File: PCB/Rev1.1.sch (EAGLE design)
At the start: 2 parts

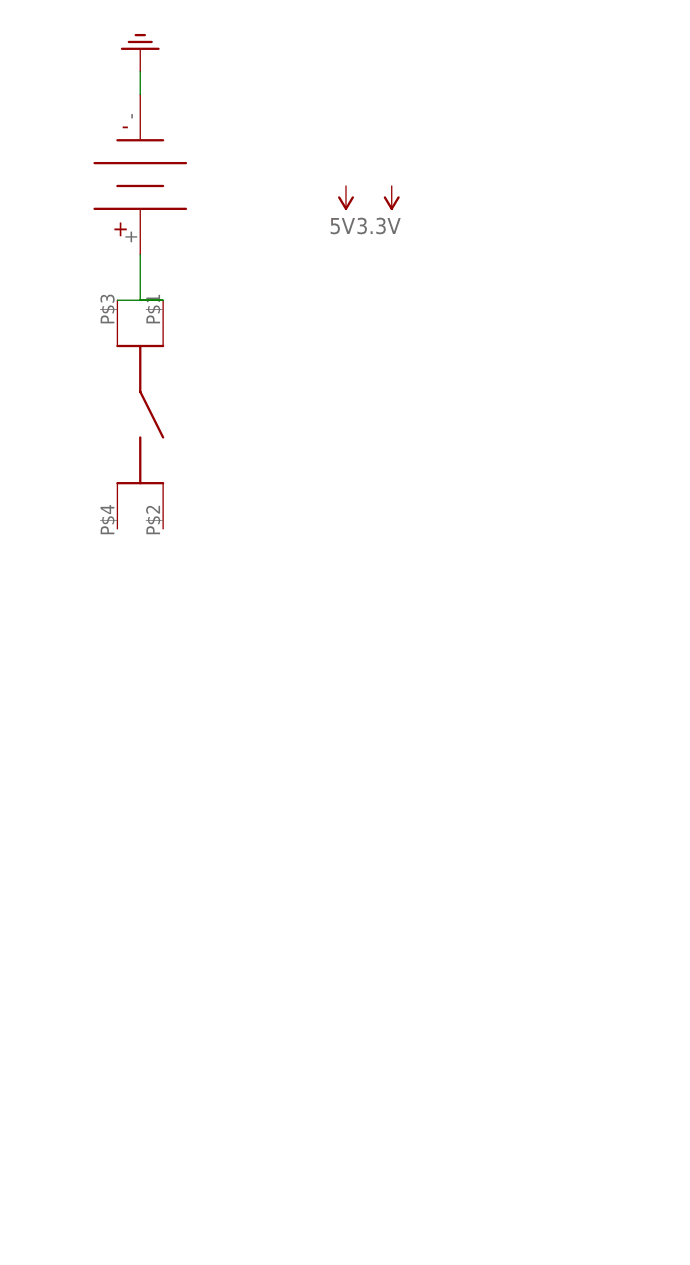
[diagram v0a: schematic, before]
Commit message: Finished power supply schematic.
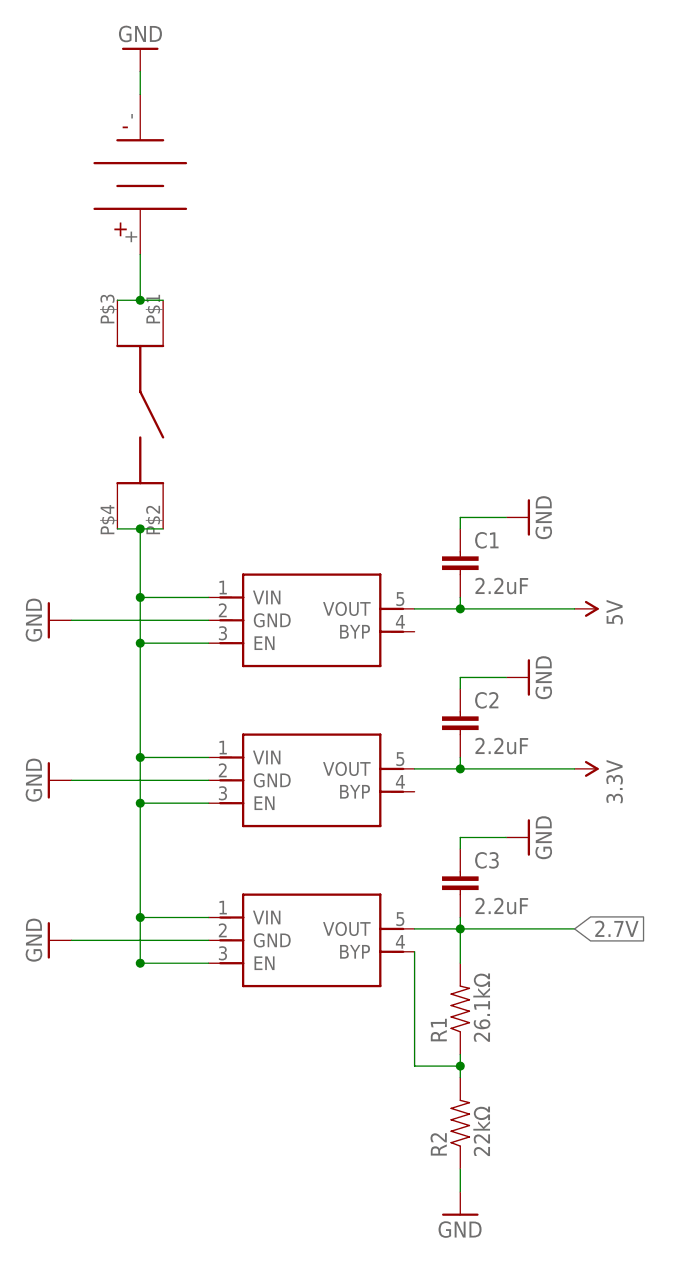
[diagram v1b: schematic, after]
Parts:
- added C1, C2, C3: 2.2uF, SparkFun-Capacitors:CAP0805
- added R1: 26.1kΩ, SparkFun-Resistors:RESISTOR0805-RES
- added R2: 22kΩ, SparkFun-Resistors:RESISTOR0805-RES
- added U$3: 5V Reg, BayouBot:SPX3819
- added U$4: 3.3V Reg, BayouBot:SPX3819
- added U$5: 2.7V Reg, BayouBot:SPX3819
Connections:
- new net 2.7V: C3.2, R1.2, U$5.VOUT
- new net 3.3V: C2.2, U$4.VOUT
- new net 5V: C1.2, U$3.VOUT
- new net N$2: U$2.P$2, U$2.P$4, U$3.EN, U$3.VIN, U$4.EN, U$4.VIN, U$5.EN, U$5.VIN
- new net N$3: R1.1, R2.2, U$5.BYP
- net GND: now also C1.1, C2.1, C3.1, R2.1, U$3.GND, U$4.GND, U$5.GND

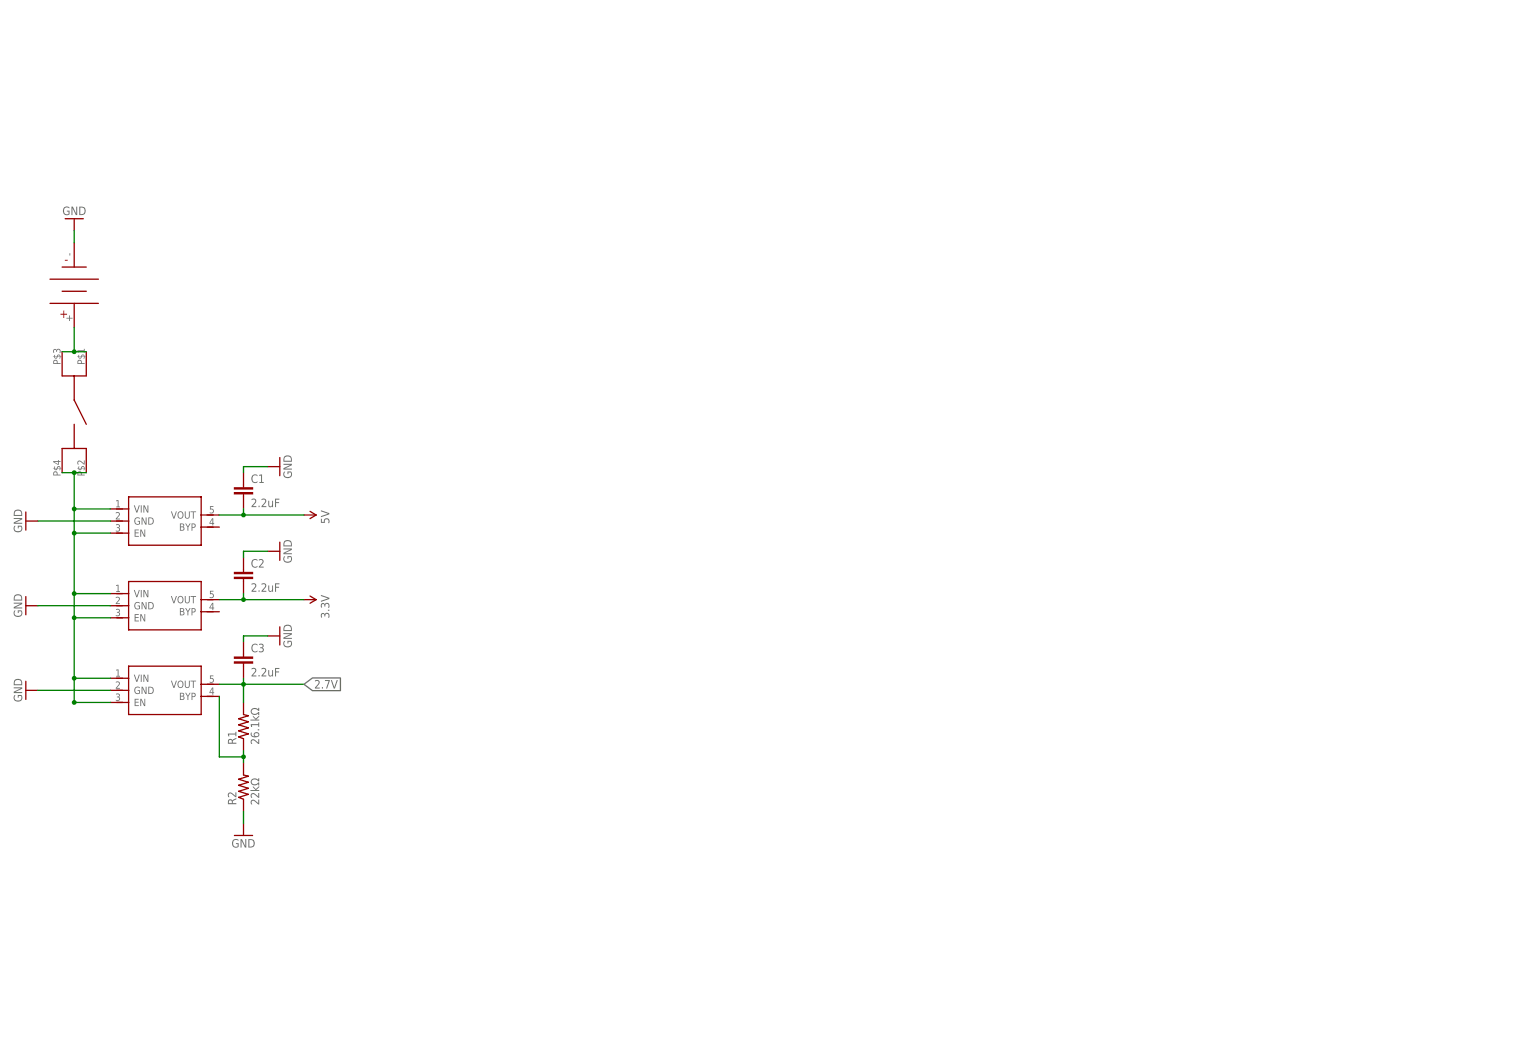
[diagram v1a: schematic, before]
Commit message: Finished schematic for next board revision.
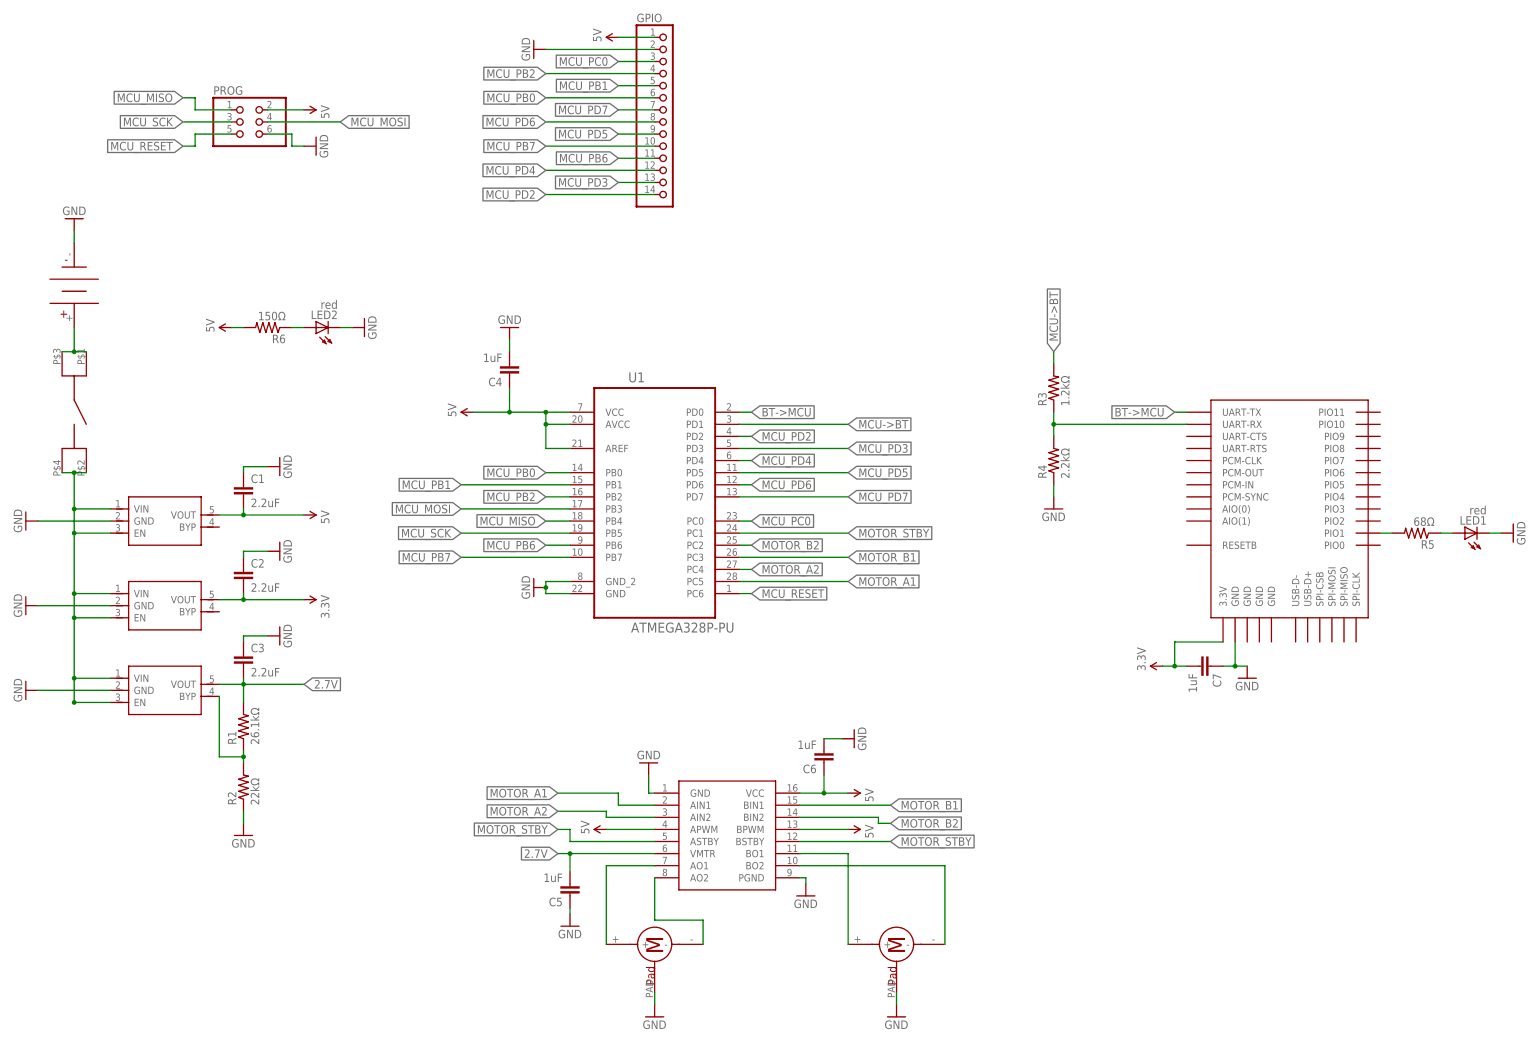
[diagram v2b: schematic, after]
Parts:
- added C4, C5, C6, C7: 1uF, SparkFun-Capacitors:CAP0805
- added GPIO: (no value), pinhead:PINHD-1X14
- added LED1, LED2: red, adafruit:LEDCHIP-LED0805
- added PROG: (no value), pinhead:PINHD-2X3
- added R3: 1.2kΩ, SparkFun-Resistors:RESISTOR0805-RES
- added R4: 2.2kΩ, SparkFun-Resistors:RESISTOR0805-RES
- added R5: 68Ω, SparkFun-Resistors:RESISTOR0805-RES
- added R6: 150Ω, SparkFun-Resistors:RESISTOR0805-RES
- added U$7, U$8: PICO_VIBE_MTR, BayouBot:PICO_VIBE_MTR
- added U1: ATMEGA328P-PU, Atmel_By_element14_Batch_1-00:ATMEGA328P-PU
- added U2: BT, BayouBot:BTM400_6B
- added U3: SMD_H-BRIDGE, BayouBot:SMD_H-BRIDGE
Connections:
- new net BT->MCU: U1.PD0, U2.UART-TX
- new net MCU->BT: R3.2, U1.PD1
- new net MCU_MISO: PROG.1, U1.PB4
- new net MCU_MOSI: PROG.4, U1.PB3
- new net MCU_PB0: GPIO.6, U1.PB0
- new net MCU_PB1: GPIO.5, U1.PB1
- new net MCU_PB2: GPIO.4, U1.PB2
- new net MCU_PB6: GPIO.11, U1.PB6
- new net MCU_PB7: GPIO.10, U1.PB7
- new net MCU_PC0: GPIO.3, U1.PC0
- new net MCU_PD2: GPIO.14, U1.PD2
- new net MCU_PD3: GPIO.13, U1.PD3
- new net MCU_PD4: GPIO.12, U1.PD4
- new net MCU_PD5: GPIO.9, U1.PD5
- new net MCU_PD6: GPIO.8, U1.PD6
- new net MCU_PD7: GPIO.7, U1.PD7
- new net MCU_RESET: PROG.5, U1.PC6
- new net MCU_SCK: PROG.3, U1.PB5
- new net MOTOR_A1: U1.PC5, U3.AIN1
- new net MOTOR_A2: U1.PC4, U3.AIN2
- new net MOTOR_B1: U1.PC3, U3.BIN1
- new net MOTOR_B2: U1.PC2, U3.BIN2
- new net MOTOR_STBY: U1.PC1, U3.ASTBY, U3.BSTBY
- new net N$10: R5.2, U2.PIO1
- new net N$11: LED1.A, R5.1
- new net N$12: LED2.A, R6.1
- new net N$4: U$7.+, U3.AO1
- new net N$5: U$7.-, U3.AO2
- new net N$6: U$8.+, U3.BO1
- new net N$7: U$8.-, U3.BO2
- new net N$8: C5.2, U3.VMTR
- new net N$9: R3.1, R4.2, U2.UART-RX
- net 3.3V: now also C7.2, U2.3.3V
- net 5V: now also C4.1, C6.1, GPIO.1, PROG.2, R6.2, U1.AREF, U1.AVCC, U1.VCC, U3.APWM, U3.BPWM, U3.VCC
- net GND: now also C4.2, C5.1, C6.2, C7.1, GPIO.2, LED1.C, LED2.C, PROG.6, R4.1, U$7.PAD, U$8.PAD, U1.GND, U1.GND_2, U2.GND@1, U3.GND, U3.PGND

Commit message: Routed new PCB version.
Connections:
- removed net N$8: C5.2, U3.VMTR
- net 2.7V: now also C5.2, U3.VMTR
- net MCU_PB0: now also GPIO.14; no longer GPIO.6
- net MCU_PB6: now also GPIO.9; no longer GPIO.11
- net MCU_PD2: now also GPIO.6; no longer GPIO.14
- net MCU_PD3: now also GPIO.7; no longer GPIO.13
- net MCU_PD4: now also GPIO.8; no longer GPIO.12
- net MCU_PD5: now also GPIO.11; no longer GPIO.9
- net MCU_PD6: now also GPIO.12; no longer GPIO.8
- net MCU_PD7: now also GPIO.13; no longer GPIO.7
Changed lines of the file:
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@@
 <setting verticaltext="up"/>
 </settings>
-<grid distance="0.1" unitdist="inch" unit="inch" style="lines" multiple="1" display="no" altdistance="0.05" altunitdist="inch" altunit="inch"/>
+<grid distance="0.1" unitdist="inch" unit="inch" style="lines" multiple="1" display="no" altdistance="0.01" altunitdist="inch" altunit="inch"/>
 <layers>
 <layer number="1" name="Top" color="4" fill="1" visible="no" active="no"/>
@@
 <parts>
 <part name="U$1" library="BayouBot" deviceset="20MM_COIN" device=""/>
-<part name="U$2" library="BayouBot" deviceset="POWER_BTN" device=""/>
 <part name="SUPPLY1" library="SparkFun-Aesthetics" deviceset="5V" device=""/>
 <part name="SUPPLY2" library="SparkFun-Aesthetics" deviceset="3.3V" device=""/>
@@
 <part name="LED2" library="adafruit" deviceset="LED" device="CHIP-LED0805" value="red"/>
 <part name="R6" library="SparkFun-Resistors" deviceset="RESISTOR" device="0805-RES" value="150Ω"/>
+<part name="U$2" library="BayouBot" deviceset="POWER_BTN" device=""/>
 </parts>
 <sheets>
@@
 <instances>
 <instance part="U$1" gate="G$1" x="22.86" y="55.88" rot="R180"/>
-<instance part="U$2" gate="G$1" x="22.86" y="30.48" rot="R270"/>
 <instance part="SUPPLY1" gate="G$1" x="71.12" y="8.89" rot="R270"/>
 <instance part="SUPPLY2" gate="G$1" x="71.12" y="-8.89" rot="R270"/>
@@
 <instance part="LED2" gate="G$1" x="73.66" y="48.26" rot="R90"/>
 <instance part="R6" gate="G$1" x="63.5" y="48.26" rot="R180"/>
+<instance part="U$2" gate="G$1" x="22.86" y="30.48" rot="R270"/>
 </instances>
 <busses>
@@
 <pinref part="U$1" gate="G$1" pin="+"/>
 <wire x1="22.86" y1="48.26" x2="22.86" y2="43.18" width="0.1524" layer="91"/>
-<pinref part="U$2" gate="G$1" pin="P$3"/>
 <wire x1="22.86" y1="43.18" x2="20.32" y2="43.18" width="0.1524" layer="91"/>
 <junction x="22.86" y="43.18"/>
+<wire x1="22.86" y1="43.18" x2="25.4" y2="43.18" width="0.1524" layer="91"/>
 <pinref part="U$2" gate="G$1" pin="P$1"/>
-<wire x1="22.86" y1="43.18" x2="25.4" y2="43.18" width="0.1524" layer="91"/>
+<pinref part="U$2" gate="G$1" pin="P$3"/>
 </segment>
 </net>
@@
 <net name="N$2" class="1">
 <segment>
-<pinref part="U$2" gate="G$1" pin="P$4"/>
-<pinref part="U$2" gate="G$1" pin="P$2"/>
 <wire x1="20.32" y1="17.78" x2="22.86" y2="17.78" width="0.1524" layer="91"/>
 <junction x="22.86" y="17.78"/>
@@
 <junction x="22.86" y="-25.4"/>
 <junction x="22.86" y="-30.48"/>
+<pinref part="U$2" gate="G$1" pin="P$2"/>
+<pinref part="U$2" gate="G$1" pin="P$4"/>
 </segment>
 </net>
@@
 <label x="124.46" y="-62.23" size="1.778" layer="95" rot="R180" xref="yes"/>
 </segment>
+<segment>
+<pinref part="U3" gate="G$1" pin="VMTR"/>
+<wire x1="124.46" y1="-62.23" x2="127" y2="-62.23" width="0.1524" layer="91"/>
+<junction x="127" y="-62.23"/>
+<wire x1="127" y1="-62.23" x2="144.78" y2="-62.23" width="0.1524" layer="91"/>
+<pinref part="C5" gate="G$1" pin="2"/>
+<wire x1="127" y1="-66.04" x2="127" y2="-62.23" width="0.1524" layer="91"/>
+</segment>
 </net>
 <net name="N$3" class="1">
@@
 </segment>
 </net>
-<net name="N$8" class="0">
-<segment>
-<pinref part="U3" gate="G$1" pin="VMTR"/>
-<wire x1="124.46" y1="-62.23" x2="127" y2="-62.23" width="0.1524" layer="91"/>
-<junction x="127" y="-62.23"/>
-<wire x1="127" y1="-62.23" x2="144.78" y2="-62.23" width="0.1524" layer="91"/>
-<pinref part="C5" gate="G$1" pin="2"/>
-<wire x1="127" y1="-66.04" x2="127" y2="-62.23" width="0.1524" layer="91"/>
-</segment>
-</net>
 <net name="MCU_PB0" class="0">
 <segment>
@@
 </segment>
 <segment>
-<pinref part="GPIO" gate="A" pin="6"/>
-<wire x1="144.78" y1="96.52" x2="121.92" y2="96.52" width="0.1524" layer="91"/>
-<label x="121.92" y="96.52" size="1.778" layer="95" rot="R180" xref="yes"/>
+<pinref part="GPIO" gate="A" pin="14"/>
+<wire x1="144.78" y1="76.2" x2="121.92" y2="76.2" width="0.1524" layer="91"/>
+<label x="121.92" y="76.2" size="1.778" layer="95" rot="R180" xref="yes"/>
 </segment>
 </net>
@@
 </segment>
 <segment>
-<pinref part="GPIO" gate="A" pin="11"/>
-<wire x1="144.78" y1="83.82" x2="137.16" y2="83.82" width="0.1524" layer="91"/>
-<label x="137.16" y="83.82" size="1.778" layer="95" rot="R180" xref="yes"/>
+<pinref part="GPIO" gate="A" pin="9"/>
+<wire x1="144.78" y1="88.9" x2="137.16" y2="88.9" width="0.1524" layer="91"/>
+<label x="137.16" y="88.9" size="1.778" layer="95" rot="R180" xref="yes"/>
 </segment>
 </net>
@@
 </segment>
 <segment>
+<pinref part="GPIO" gate="A" pin="13"/>
+<wire x1="144.78" y1="78.74" x2="137.16" y2="78.74" width="0.1524" layer="91"/>
+<label x="137.16" y="78.74" size="1.778" layer="95" rot="R180" xref="yes"/>
+</segment>
+</net>
+<net name="MCU_PD6" class="0">
+<segment>
+<pinref part="U1" gate="A" pin="PD6"/>
+<wire x1="162.56" y1="15.24" x2="165.1" y2="15.24" width="0.1524" layer="91"/>
+<label x="165.1" y="15.24" size="1.778" layer="95" xref="yes"/>
+</segment>
+<segment>
+<pinref part="GPIO" gate="A" pin="12"/>
+<wire x1="144.78" y1="81.28" x2="121.92" y2="81.28" width="0.1524" layer="91"/>
+<label x="121.92" y="81.28" size="1.778" layer="95" rot="R180" xref="yes"/>
+</segment>
+</net>
+<net name="MCU_PD5" class="0">
+<segment>
+<pinref part="U1" gate="A" pin="PD5"/>
+<wire x1="162.56" y1="17.78" x2="185.42" y2="17.78" width="0.1524" layer="91"/>
+<label x="185.42" y="17.78" size="1.778" layer="95" xref="yes"/>
+</segment>
+<segment>
+<pinref part="GPIO" gate="A" pin="11"/>
+<wire x1="144.78" y1="83.82" x2="137.16" y2="83.82" width="0.1524" layer="91"/>
+<label x="137.16" y="83.82" size="1.778" layer="95" rot="R180" xref="yes"/>
+</segment>
+</net>
+<net name="MCU_PD4" class="0">
+<segment>
+<pinref part="U1" gate="A" pin="PD4"/>
+<wire x1="162.56" y1="20.32" x2="165.1" y2="20.32" width="0.1524" layer="91"/>
+<label x="165.1" y="20.32" size="1.778" layer="95" xref="yes"/>
+</segment>
+<segment>
+<pinref part="GPIO" gate="A" pin="8"/>
+<wire x1="144.78" y1="91.44" x2="121.92" y2="91.44" width="0.1524" layer="91"/>
+<label x="121.92" y="91.44" size="1.778" layer="95" rot="R180" xref="yes"/>
+</segment>
+</net>
+<net name="MCU_PD3" class="0">
+<segment>
+<pinref part="U1" gate="A" pin="PD3"/>
+<wire x1="162.56" y1="22.86" x2="185.42" y2="22.86" width="0.1524" layer="91"/>
+<label x="185.42" y="22.86" size="1.778" layer="95" xref="yes"/>
+</segment>
+<segment>
 <pinref part="GPIO" gate="A" pin="7"/>
 <wire x1="144.78" y1="93.98" x2="137.16" y2="93.98" width="0.1524" layer="91"/>
@@
 </segment>
 </net>
-<net name="MCU_PD6" class="0">
-<segment>
-<pinref part="U1" gate="A" pin="PD6"/>
-<wire x1="162.56" y1="15.24" x2="165.1" y2="15.24" width="0.1524" layer="91"/>
-<label x="165.1" y="15.24" size="1.778" layer="95" xref="yes"/>
-</segment>
-<segment>
-<pinref part="GPIO" gate="A" pin="8"/>
-<wire x1="144.78" y1="91.44" x2="121.92" y2="91.44" width="0.1524" layer="91"/>
-<label x="121.92" y="91.44" size="1.778" layer="95" rot="R180" xref="yes"/>
-</segment>
-</net>
-<net name="MCU_PD5" class="0">
-<segment>
-<pinref part="U1" gate="A" pin="PD5"/>
-<wire x1="162.56" y1="17.78" x2="185.42" y2="17.78" width="0.1524" layer="91"/>
-<label x="185.42" y="17.78" size="1.778" layer="95" xref="yes"/>
-</segment>
-<segment>
-<pinref part="GPIO" gate="A" pin="9"/>
-<wire x1="144.78" y1="88.9" x2="137.16" y2="88.9" width="0.1524" layer="91"/>
-<label x="137.16" y="88.9" size="1.778" layer="95" rot="R180" xref="yes"/>
-</segment>
-</net>
-<net name="MCU_PD4" class="0">
-<segment>
-<pinref part="U1" gate="A" pin="PD4"/>
-<wire x1="162.56" y1="20.32" x2="165.1" y2="20.32" width="0.1524" layer="91"/>
-<label x="165.1" y="20.32" size="1.778" layer="95" xref="yes"/>
-</segment>
-<segment>
-<pinref part="GPIO" gate="A" pin="12"/>
-<wire x1="144.78" y1="81.28" x2="121.92" y2="81.28" width="0.1524" layer="91"/>
-<label x="121.92" y="81.28" size="1.778" layer="95" rot="R180" xref="yes"/>
-</segment>
-</net>
-<net name="MCU_PD3" class="0">
-<segment>
-<pinref part="U1" gate="A" pin="PD3"/>
-<wire x1="162.56" y1="22.86" x2="185.42" y2="22.86" width="0.1524" layer="91"/>
-<label x="185.42" y="22.86" size="1.778" layer="95" xref="yes"/>
-</segment>
-<segment>
-<pinref part="GPIO" gate="A" pin="13"/>
-<wire x1="144.78" y1="78.74" x2="137.16" y2="78.74" width="0.1524" layer="91"/>
-<label x="137.16" y="78.74" size="1.778" layer="95" rot="R180" xref="yes"/>
-</segment>
-</net>
 <net name="MCU_PD2" class="0">
 <segment>
@@
 </segment>
 <segment>
-<pinref part="GPIO" gate="A" pin="14"/>
-<wire x1="144.78" y1="76.2" x2="121.92" y2="76.2" width="0.1524" layer="91"/>
-<label x="121.92" y="76.2" size="1.778" layer="95" rot="R180" xref="yes"/>
-</segment>
-</net>
+<pinref part="GPIO" gate="A" pin="6"/>
+<wire x1="144.78" y1="96.52" x2="121.92" y2="96.52" width="0.1524" layer="91"/>
+<label x="121.92" y="96.52" size="1.778" layer="95" rot="R180" xref="yes"/>
+</segment>
+</net>
